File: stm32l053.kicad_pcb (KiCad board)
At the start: 2 copper layers, 23.9 x 59.4 mm, 17 parts, among them P1 SWD, P2 CONN_01X23, P3 CONN_01X23, P5 Ext Xtal, SW1 RESET, U1 STM32_LQFP64

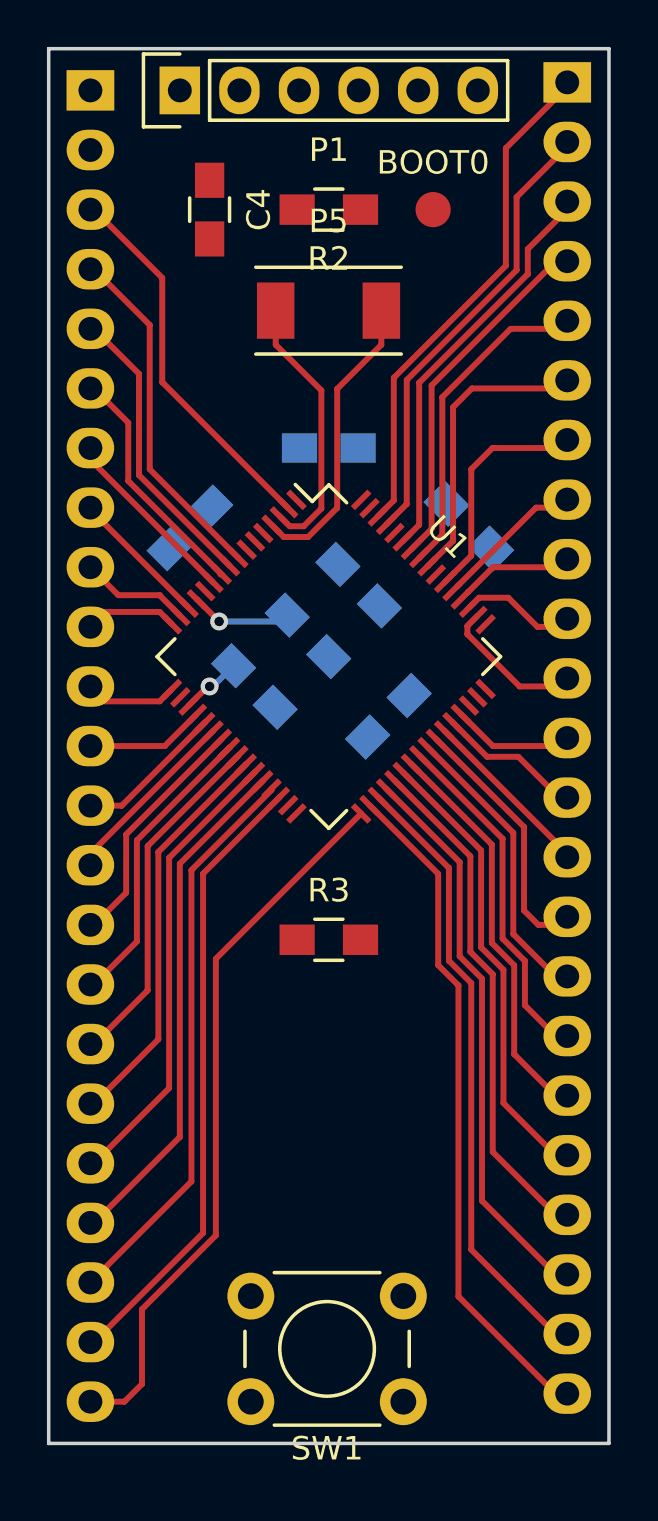
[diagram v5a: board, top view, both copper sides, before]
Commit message: SWO header
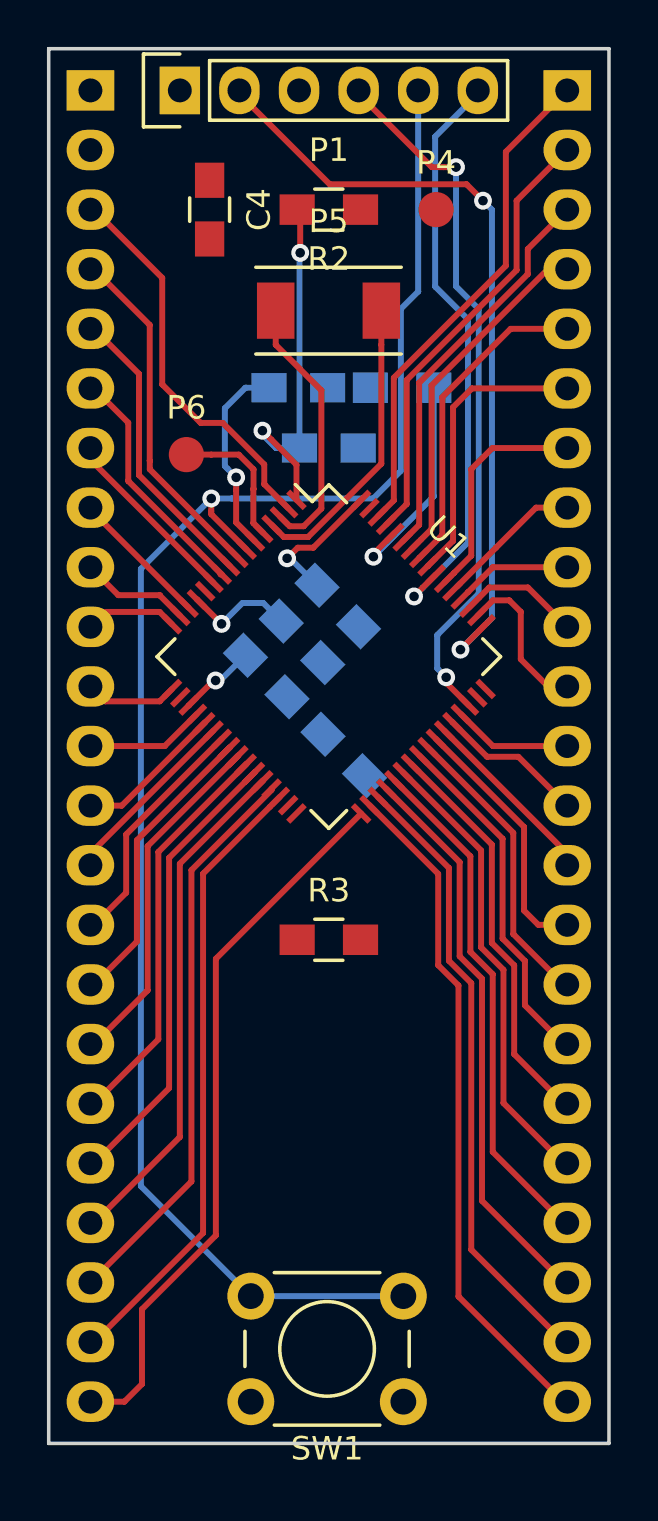
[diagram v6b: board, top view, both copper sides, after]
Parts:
- removed BOOT0: CONN_01X01, Measurement_Points:Measurement_Point_Round-SMD-Pad_Small
- added P4: BOOT0, Measurement_Points:Measurement_Point_Round-SMD-Pad_Small, F.Cu at (154.4, 86.4)
- added P6: MCO, Measurement_Points:Measurement_Point_Round-SMD-Pad_Small, F.Cu at (143.8, 96.8)
- moved C2 7.55 mm to (148.6, 94.0), turned to 0 degrees
- moved R1 6.55 mm to (153.0, 94.0), turned to 180 degrees
- moved C1 2.52 mm to (150.5, 109.6), turned to 135 degrees
- moved C7 1.26 mm to (150.2, 103.3)
- moved C6 0.68 mm to (147.2, 106.2)
- moved C5 0.36 mm to (148.7, 104.8)
- moved P3 0.34 mm to (160.0, 81.3)
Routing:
- net NRST: track 0.00 -> 71.6 mm, vias 0 -> 1
- net SWCLK: track 0.00 -> 33.8 mm, vias 0 -> 2
- net SWDIO: track 0.00 -> 30.2 mm, vias 0 -> 2
- net SWO: track 0.00 -> 25.2 mm, vias 0 -> 1
- net /VLCD: track 0.10 -> 15.9 mm, vias 0 -> 2
- net BOOT0: track 0.00 -> 9.64 mm, vias 0 -> 1
- net Net-(C2-Pad1): track 0.00 -> 8.44 mm, vias 0 -> 1
- net VDD: track 6.97 -> 14.4 mm, vias 2 -> 3
- net MCO: track 0.00 -> 6.01 mm
- net /PA15: track 6.13 -> 6.81 mm
- net /PC13: track 16.3 -> 16.9 mm

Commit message: VDD connected
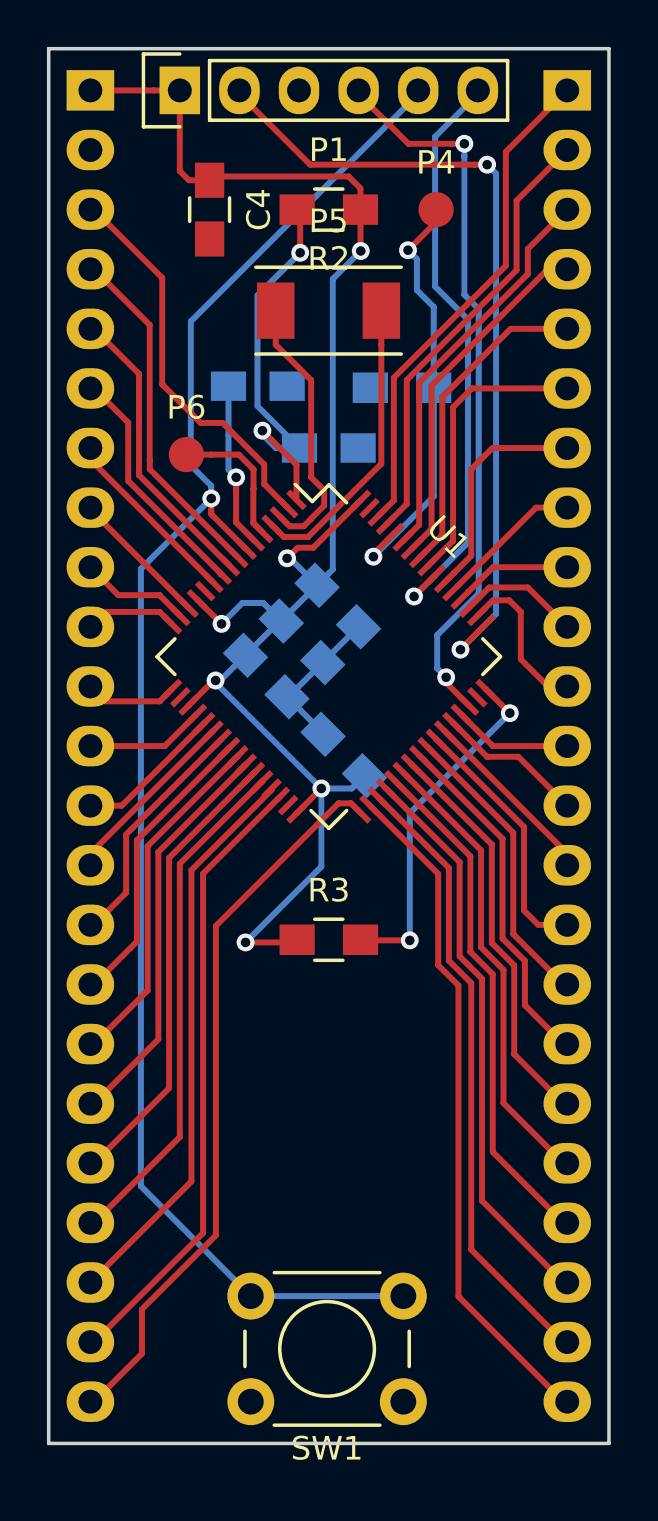
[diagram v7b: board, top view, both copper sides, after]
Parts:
- moved C2 1.73 mm to (146.8, 93.9)
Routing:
- net VDD: track 14.4 -> 72.0 mm, vias 3 -> 6
- net /VDD_USB: track 0.00 -> 15.0 mm, vias 0 -> 2
- net BOOT0: track 9.64 -> 18.2 mm, vias 1 -> 2
- net Earth: track 0.06 -> 6.52 mm
- net NRST: track 71.6 -> 68.3 mm
- net /VLCD: track 15.9 -> 17.3 mm
- net Net-(C2-Pad1): track 8.44 -> 7.08 mm
- net SWCLK: track 33.8 -> 34.9 mm
- net SWDIO: track 30.2 -> 31.0 mm
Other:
- net class Wide: trace_width 0.4064 -> 0.3556

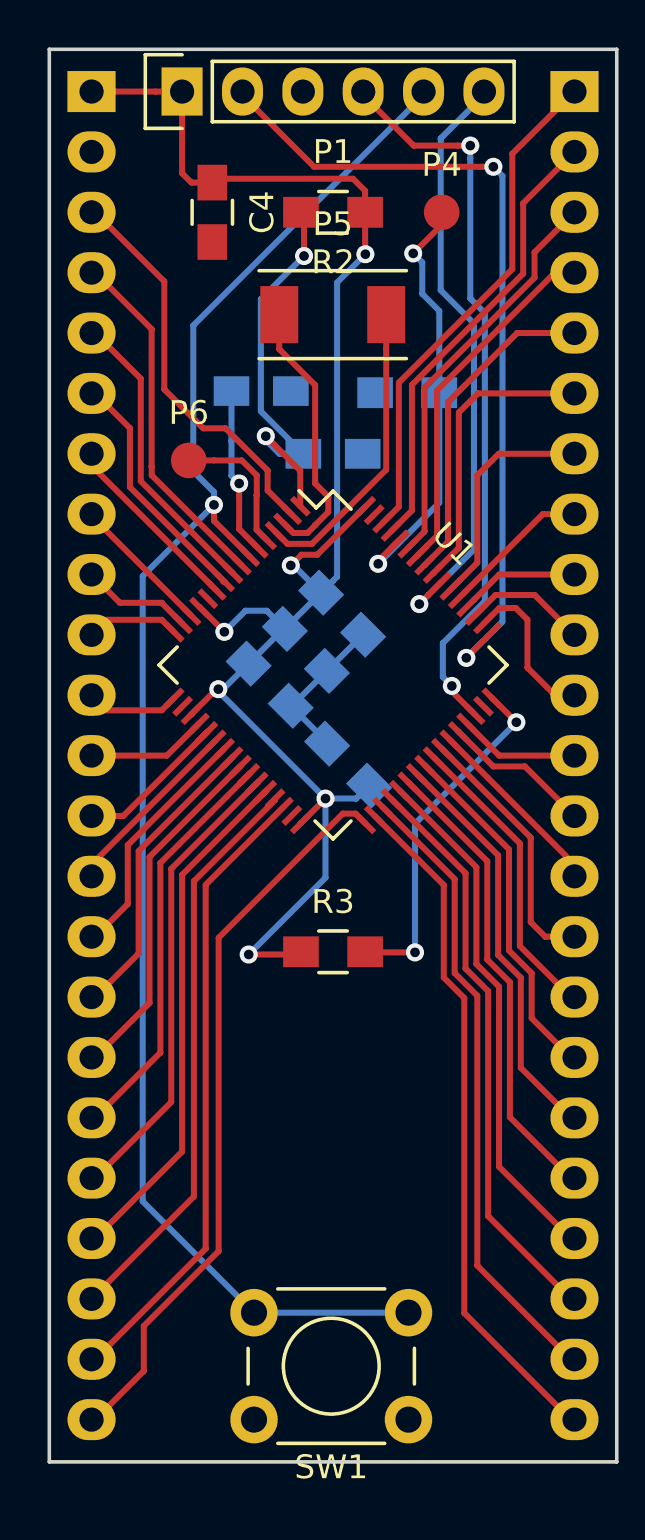
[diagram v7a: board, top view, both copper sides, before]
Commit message: Earth connected
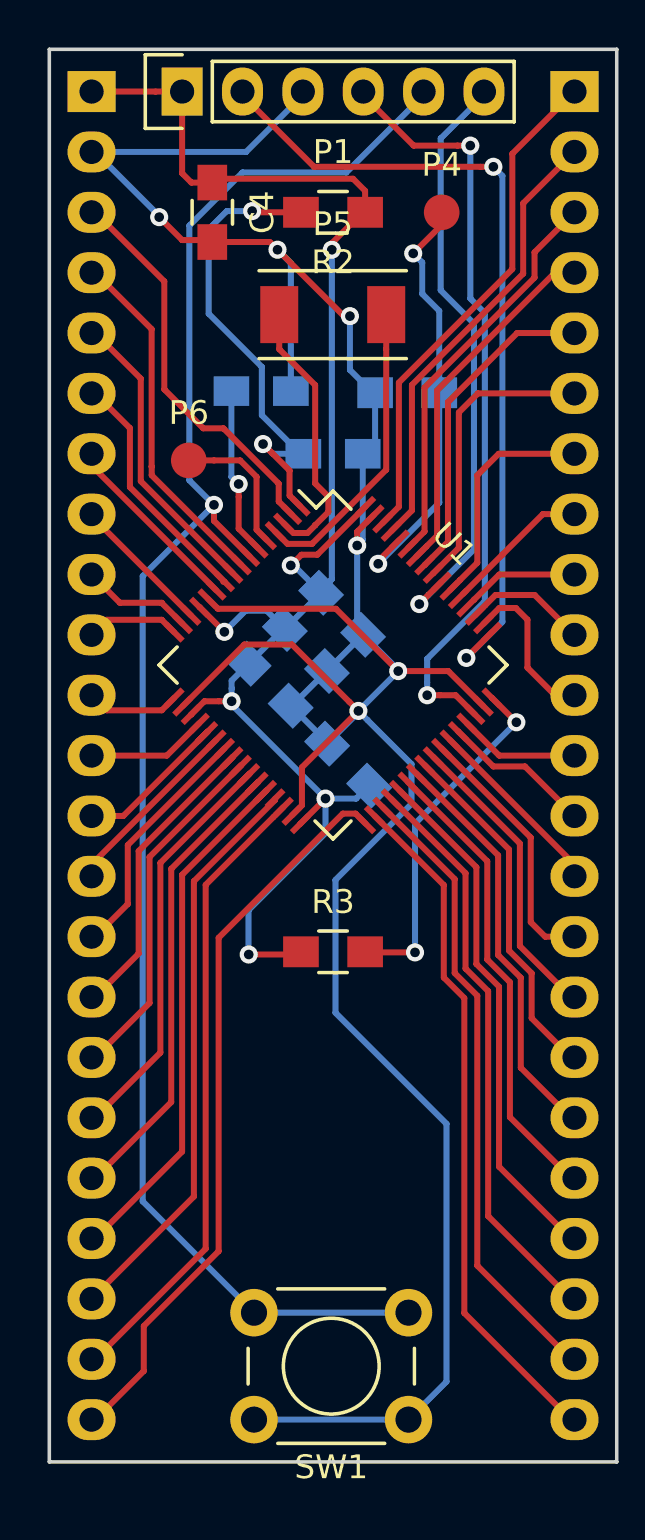
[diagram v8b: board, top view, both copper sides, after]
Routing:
- net Earth: track 6.52 -> 128.8 mm, vias 0 -> 6
- net /VLCD: track 17.3 -> 20.5 mm
- net NRST: track 68.3 -> 71.0 mm
- net SWDIO: track 31.0 -> 32.3 mm
